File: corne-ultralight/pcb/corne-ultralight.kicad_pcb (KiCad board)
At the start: 2 copper layers, 275.5 x 105.6 mm, 132 parts, among them J2 OLED, J5 Breakaway_Tabs, J7 OLED, SW1 SW_PUSH, SW10 SW_PUSH, SW11 SW_PUSH, SW12 SW_PUSH, SW13 SW_PUSH, SW14 SW_PUSH, SW15 SW_PUSH, SW16 SW_PUSH, SW17 SW_PUSH, SW18 SW_PUSH, SW19 SW_PUSH, SW2 SW_PUSH, SW20 SW_PUSH, SW21 SW_PUSH, SW22 SW_PUSH, SW23 SW_PUSH, SW24 SW_PUSH, SW25 SW_PUSH, SW26 SW_PUSH, SW27 SW_PUSH, SW28 SW_PUSH, SW29 SW_PUSH, SW3 SW_PUSH, SW30 SW_PUSH, SW31 SW_PUSH, SW32 SW_PUSH, SW33 SW_PUSH, SW34 SW_PUSH, SW35 SW_PUSH, SW36 SW_PUSH, SW37 SW_PUSH, SW38 SW_PUSH, SW39 SW_PUSH, SW4 SW_PUSH, SW40 SW_PUSH, SW41 SW_PUSH, SW42 SW_PUSH, SW5 SW_PUSH, SW6 SW_PUSH, SW7 SW_PUSH, SW8 SW_PUSH, SW9 SW_PUSH, U1 ProMicro, U2 ProMicro

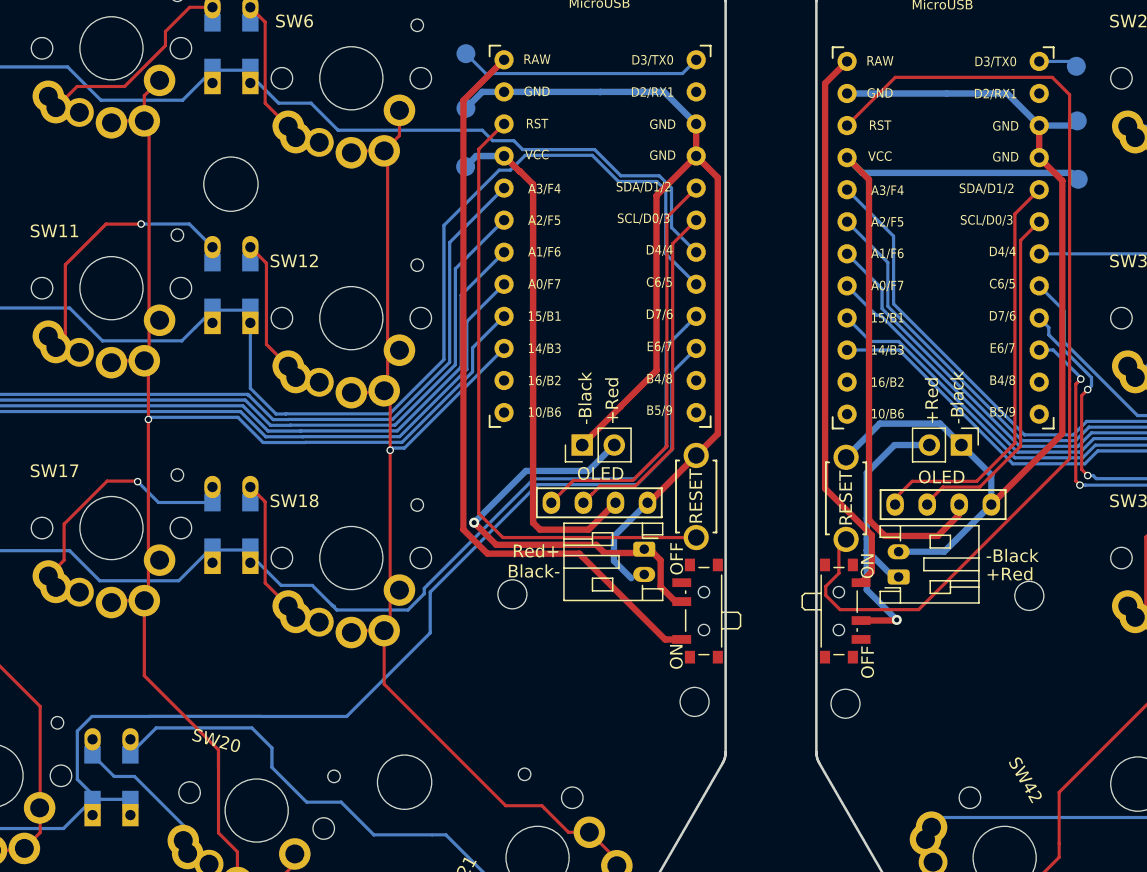
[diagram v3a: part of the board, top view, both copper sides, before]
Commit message: Switch to nice!view display header.
* Route extra pin and move header to be centered for
  nice!view display support.
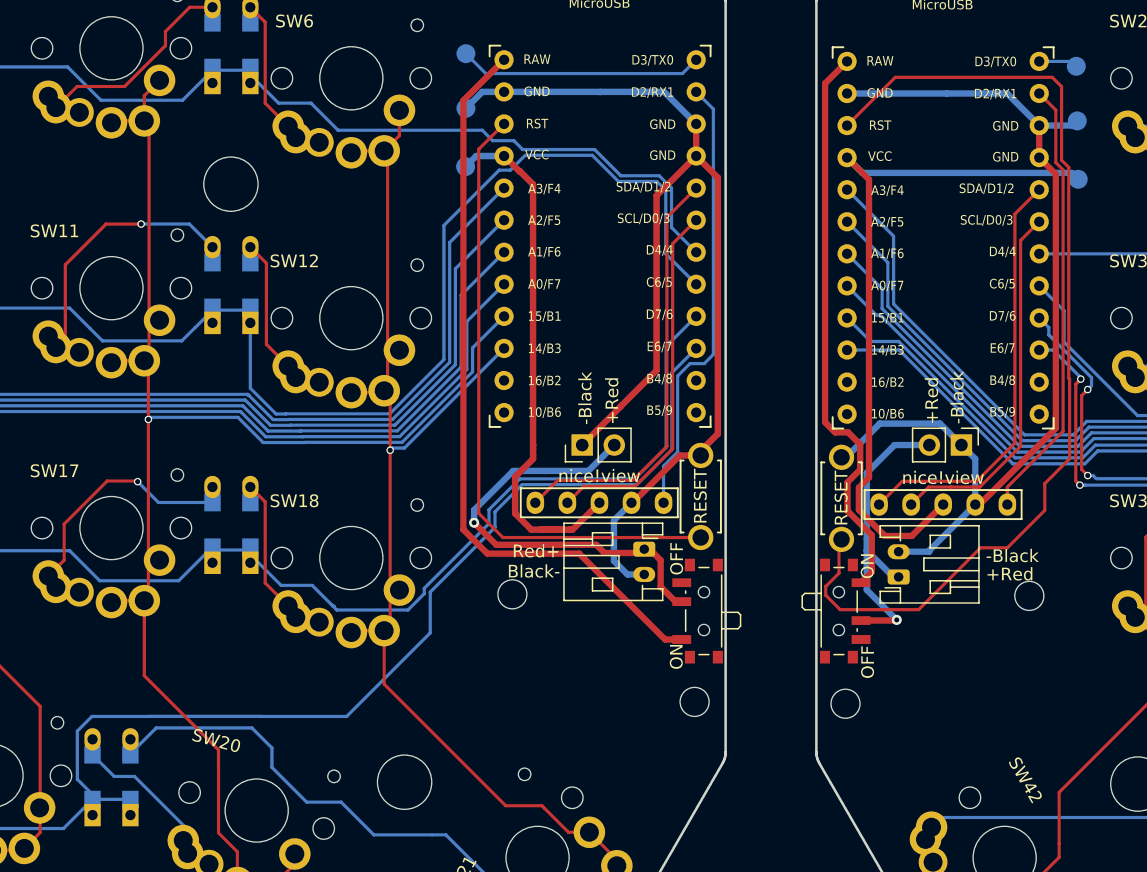
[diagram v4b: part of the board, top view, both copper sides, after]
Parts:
- J2, J7: footprint kbd:OLED_1side -> nice_view:nice_view_1side
- moved J2 1.27 mm to (131.8, 77.2)
- moved J7 1.27 mm to (159.0, 77.3)
- moved RSW2 0.36 mm to (156.0, 76.8)
- moved RSW1 0.36 mm to (144.9, 76.7)
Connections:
- U1 pad 2: unconnected-(U1-Pad2) -> CS
- U2 pad 2: unconnected-(U2-Pad2) -> CS_r
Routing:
- net CS: track 0.00 -> 35.4 mm
- net CS_r: track 0.00 -> 35.2 mm
- net VCC: track 41.1 -> 43.1 mm
- net GND: track 87.2 -> 88.9 mm
- net GNDA: track 78.1 -> 76.6 mm
- net +BATTA: track 43.9 -> 45.3 mm
- net SCL: track 27.7 -> 29.0 mm
- net SDA: track 32.4 -> 33.7 mm
- net reset_r: track 78.4 -> 79.7 mm
- net VDD: track 57.7 -> 56.5 mm
- net SCL_r: track 27.9 -> 29.0 mm
- net SDA_r: track 32.7 -> 33.6 mm
- net row3: track 97.3 -> 98.1 mm
- net row2: track 157.9 -> 158.6 mm
- net Net-(BATJ1-Pad2): track 33.9 -> 34.5 mm

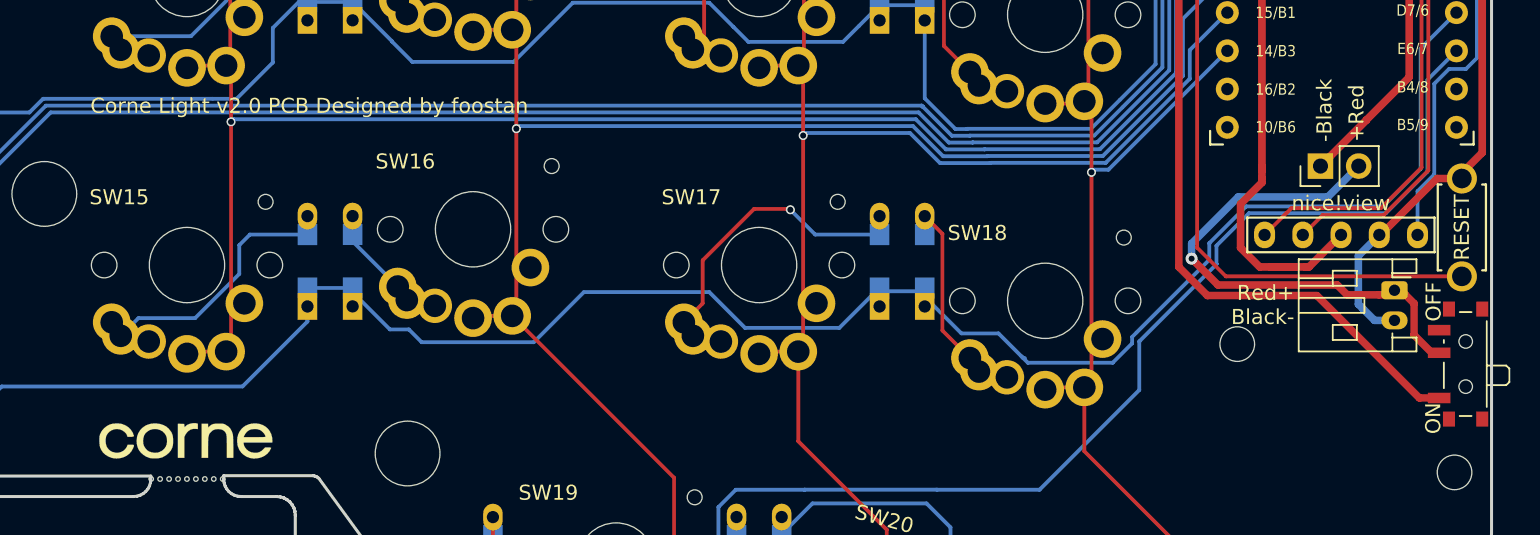
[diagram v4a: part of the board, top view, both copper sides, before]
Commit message: Consistent power switch on/off direction.
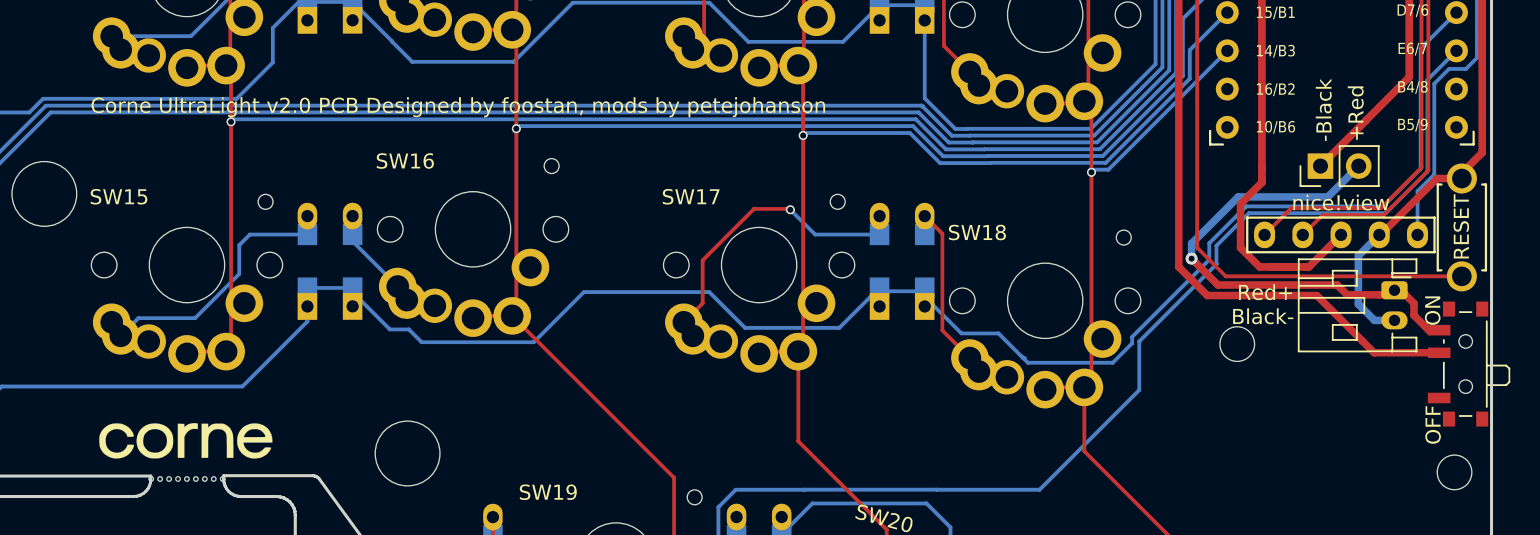
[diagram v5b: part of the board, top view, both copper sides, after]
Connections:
- PSW1 pad 1: +BATT -> unconnected-(PSW1-Pad1)
- PSW1 pad 2: Net-(BATJ1-Pad2) -> +BATT
- PSW1 pad 3: (no net) -> Net-(BATJ1-Pad2)
- PSW2 pad 3: (no net) -> unconnected-(PSW2-Pad3)
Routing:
- net Net-(BATJ1-Pad2): track 34.5 -> 33.1 mm
- net +BATT: track 59.4 -> 58.2 mm
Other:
- board text added: "Corne UltraLight v2.0 PCB Designed by foostan, mods by petejohanson"
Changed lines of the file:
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@@
   (net 87 "+BATTA")
   (net 88 "Net-(BATJ3-Pad2)")
+  (net 89 "unconnected-(PSW1-Pad1)")
+  (net 90 "unconnected-(PSW2-Pad3)")
   (footprint "kbd:ResetSW_1side" (layer "F.Cu")
     (at 156.0125 76.817432 -90)
@@
     (pad "2" smd rect (at 0.75 -1.43 270) (size 0.7 1.5) (layers "F.Cu" "F.Paste" "F.Mask")
       (net 88 "Net-(BATJ3-Pad2)") (pinfunction "B") (pintype "passive"))
-    (pad "3" smd rect (at 2.25 -1.43 270) (size 0.7 1.5) (layers "F.Cu" "F.Paste" "F.Mask"))
+    (pad "3" smd rect (at 2.25 -1.43 270) (size 0.7 1.5) (layers "F.Cu" "F.Paste" "F.Mask")
+      (net 90 "unconnected-(PSW2-Pad3)") (pinfunction "C") (pintype "passive+no_connect"))
     (model "${KICAD6_3DMODEL_DIR}/Button_Switch_SMD.3dshapes/SW_SPDT_PCM12.wrl"
       (offset (xyz 0 0 0))
@@
     (pad "" np_thru_hole circle (at -1.5 0.33 90) (size 0.9 0.9) (drill 0.9) (layers *.Cu *.Mask))
     (pad "1" smd rect (at -2.25 -1.43 90) (size 0.7 1.5) (layers "F.Cu" "F.Paste" "F.Mask")
-      (net 38 "+BATT") (pinfunction "A") (pintype "passive"))
+      (net 89 "unconnected-(PSW1-Pad1)") (pinfunction "A") (pintype "passive+no_connect"))
     (pad "2" smd rect (at 0.75 -1.43 90) (size 0.7 1.5) (layers "F.Cu" "F.Paste" "F.Mask")
-      (net 37 "Net-(BATJ1-Pad2)") (pinfunction "B") (pintype "passive"))
-    (pad "3" smd rect (at 2.25 -1.43 90) (size 0.7 1.5) (layers "F.Cu" "F.Paste" "F.Mask"))
+      (net 38 "+BATT") (pinfunction "B") (pintype "passive"))
+    (pad "3" smd rect (at 2.25 -1.43 90) (size 0.7 1.5) (layers "F.Cu" "F.Paste" "F.Mask")
+      (net 37 "Net-(BATJ1-Pad2)") (pinfunction "C") (pintype "passive"))
     (model "${KICAD6_3DMODEL_DIR}/Button_Switch_SMD.3dshapes/SW_SPDT_PCM12.wrl"
       (offset (xyz 0 0 0))
@@
     (effects (font (size 1 1) (thickness 0.125)) (justify left))
   )
-  (gr_text "Corne Light v2.0 PCB Designed by foostan" (at 53.7675 68.6) (layer "F.SilkS")
+  (gr_text "Corne UltraLight v2.0 PCB Designed by foostan, mods by petejohanson" (at 53.7675 68.6) (layer "F.SilkS")
     (effects (font (size 1 1) (thickness 0.125)) (justify left))
   )
@@
     (effects (font (size 1 1) (thickness 0.15)) (justify left))
   )
-  (gr_text "ON" (at 142.9625 88.295 90) (layer "F.SilkS")
-    (effects (font (size 1 1) (thickness 0.15)) (justify right))
+  (gr_text "ON" (at 142.9625 83.22 90) (layer "F.SilkS")
+    (effects (font (size 1 1) (thickness 0.15)) (justify left))
   )
   (gr_text "Black-" (at 133.7375 82.62) (layer "F.SilkS")
@@
     (effects (font (size 1 1) (thickness 0.15)) (justify left))
   )
-  (gr_text "OFF" (at 142.9875 80.27 90) (layer "F.SilkS")
-    (effects (font (size 1 1) (thickness 0.15)) (justify right))
+  (gr_text "OFF" (at 142.9875 91.12 90) (layer "F.SilkS")
+    (effects (font (size 1 1) (thickness 0.15)) (justify left))
   )
   (segment (start 30.1875 48.916875) (end 30.1875 47.691875) (width 0.25) (layer "B.Cu") (net 1))
@@
   (segment (start 144.5039 52.242) (end 142.1845 54.5614) (width 0.254) (layer "F.Cu") (net 36))
   (segment (start 133.5325 75.394) (end 131.7585 77.168) (width 0.254) (layer "F.Cu") (net 36))
-  (segment (start 141.6875 83.82) (end 142.8625 84.995) (width 0.5) (layer "F.Cu") (net 37))
   (segment (start 136.59002 80.49752) (end 128.66502 80.49752) (width 0.5) (layer "F.Cu") (net 37))
   (segment (start 139.3625 81.145) (end 137.2375 81.145) (width 0.5) (layer "F.Cu") (net 37))
+  (segment (start 142.6625 83.495) (end 141.6875 82.52) (width 0.5) (layer "F.Cu") (net 37))
   (segment (start 139.3625 81.145) (end 141.1125 81.145) (width 0.5) (layer "F.Cu") (net 37))
-  (segment (start 142.8625 84.995) (end 143.3575 84.995) (width 0.5) (layer "F.Cu") (net 37))
-  (segment (start 141.6875 81.72) (end 141.6875 83.82) (width 0.5) (layer "F.Cu") (net 37))
   (segment (start 141.1125 81.145) (end 141.6875 81.72) (width 0.5) (layer "F.Cu") (net 37))
+  (segment (start 141.6875 81.72) (end 141.6875 82.52) (width 0.5) (layer "F.Cu") (net 37))
   (segment (start 137.2375 81.145) (end 136.59002 80.49752) (width 0.5) (layer "F.Cu") (net 37))
+  (segment (start 143.3575 83.495) (end 142.6625 83.495) (width 0.5) (layer "F.Cu") (net 37))
   (segment (start 128.66502 80.49752) (end 126.9125 78.745) (width 0.5) (layer "F.Cu") (net 37))
   (via (at 126.9125 78.745) (size 0.8) (drill 0.4) (layers "F.Cu" "B.Cu") (net 37))
@@
   (segment (start 135.9625 74.645) (end 138.0125 72.595) (width 0.5) (layer "B.Cu") (net 37))
   (segment (start 135.23954 81.19704) (end 127.96246 81.19704) (width 0.5) (layer "F.Cu") (net 38))
+  (segment (start 143.3575 84.995) (end 139.0375 84.995) (width 0.5) (layer "F.Cu") (net 38))
   (segment (start 127.96246 81.19704) (end 126.062989 79.297569) (width 0.5) (layer "F.Cu") (net 38))
-  (segment (start 143.3575 87.995) (end 142.0375 87.995) (width 0.5) (layer "F.Cu") (net 38))
   (segment (start 126.062989 45.302911) (end 129.2839 42.082) (width 0.5) (layer "F.Cu") (net 38))
-  (segment (start 142.0375 87.995) (end 135.23954 81.19704) (width 0.5) (layer "F.Cu") (net 38))
+  (segment (start 139.0375 84.995) (end 138.275 84.2325) (width 0.5) (layer "F.Cu") (net 38))
   (segment (start 126.062989 79.297569) (end 126.062989 45.302911) (width 0.5) (layer "F.Cu") (net 38))
+  (segment (start 138.275 84.2325) (end 135.23954 81.19704) (width 0.5) (layer "F.Cu") (net 38))
   (segment (start 273.684847 49.720432) (end 270.684847 46.720432) (width 0.25) (layer "F.Cu") (net 41))
   (segment (start 270.684847 46.720432) (end 270.684847 42.920432) (width 0.25) (layer "F.Cu") (net 41))

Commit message: Fix hybrid footprint for 5-pin MX switches.
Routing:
- net Net-(D8-Pad2): track 22.1 -> 8.17 mm
- net col0: track 181.9 -> 177.7 mm
- net col1_r: track 165.8 -> 161.7 mm
- net col4: track 116.4 -> 112.2 mm
- net Net-(D29-Pad2): track 27.1 -> 23.0 mm
- net col2_r: track 147.4 -> 143.5 mm
- net col5_r: track 119.5 -> 115.8 mm
- net col4_r: track 133.0 -> 129.4 mm
- net col5: track 94.4 -> 91.2 mm
- net row1_r: track 136.6 -> 139.8 mm
- net col3_r: track 152.8 -> 149.9 mm
- net col1: track 150.3 -> 147.7 mm
- net col3: track 135.1 -> 132.6 mm
- net col0_r: track 188.1 -> 185.7 mm
- net col2: track 126.5 -> 124.1 mm
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
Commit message: feat: switch to hotswap
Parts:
- SW1, SW10, SW11, SW12, SW13, SW14, SW15, SW16, SW17, SW18, SW19, SW2, SW20, SW22, SW23, SW24, SW25, SW26, SW27, SW28, SW29, SW3, SW30, SW31, SW32, SW33, SW34, SW35, SW36, SW37, SW38, SW39, SW4, SW40, SW41, SW5, SW6, SW7, SW8, SW9: footprint gateron-ks27:gateron-ks27-choc-v1-mx -> PCM_Switch_Keyboard_Hotswap_Kailh:SW_Hotswap_Kailh_Choc_V1V2
- SW21, SW42: footprint gateron-ks27:gateron-ks27-choc-v1-mx-1.5u -> PCM_Switch_Keyboard_Hotswap_Kailh:SW_Hotswap_Kailh_Choc_V1V2_1.50u
- moved D16 4.97 mm to (71.2, 73.9)
- moved D10 4.97 mm to (71.2, 54.9)
- moved D4 4.97 mm to (71.2, 35.9)
- moved TP6 3.53 mm to (174.7, 50.4)
- moved D34 2.98 mm to (270.7, 80.9)
- moved D38 2.98 mm to (194.7, 75.9)
- moved D28 2.98 mm to (270.7, 61.9)
- moved D22 2.98 mm to (270.7, 42.9)
- moved D2 2.98 mm to (33.2, 42.9)
- moved D19 2.97 mm to (80.7, 95.9)
- moved D41 2.97 mm to (204.2, 95.9)
- moved D8 2.75 mm to (33.2, 62.2)
- moved D30 2.70 mm to (232.7, 57.2)
- moved D14 2.70 mm to (33.2, 81.2)
- moved D36 2.48 mm to (232.7, 76.4)
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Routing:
- net row1: track 168.5 -> 147.9 mm
- net col0: track 177.7 -> 163.3 mm, vias 1 -> 4
- net Net-(D37-Pad2): track 14.2 -> 24.3 mm
- net row3: track 97.9 -> 88.4 mm
- net Net-(D23-Pad2): track 18.0 -> 27.3 mm, vias 0 -> 1
- net Net-(D5-Pad2): track 17.6 -> 26.3 mm, vias 0 -> 2
- net row2: track 157.3 -> 148.9 mm
- net col3_r: track 149.9 -> 158.1 mm, vias 1 -> 5
- net col4_r: track 129.4 -> 137.4 mm, vias 1 -> 5
- net Net-(D25-Pad2): track 17.3 -> 24.3 mm
- net Net-(D31-Pad2): track 17.4 -> 24.3 mm
- net col1: track 147.7 -> 140.9 mm, vias 1 -> 4
- net col0_r: track 185.7 -> 192.5 mm, vias 1 -> 4
- net Net-(D17-Pad2): track 19.7 -> 26.0 mm, vias 1 -> 2
- net col5: track 91.2 -> 85.4 mm, vias 1 -> 5
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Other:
- outline, holes or cut-outs redrawn

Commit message: fix: correct the routing problem
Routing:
- net col4_r: track 137.4 -> 127.7 mm, vias 5 -> 7
- net col5_r: track 120.2 -> 111.2 mm, vias 5 -> 7
- net col0_r: track 192.5 -> 183.7 mm, vias 4 -> 5
- net col3_r: track 158.1 -> 150.0 mm, vias 5 -> 7
- net col1_r: track 165.1 -> 157.7 mm, vias 4 -> 5
- net col3: track 129.8 -> 122.5 mm, vias 5 -> 7
- net col2: track 123.0 -> 116.3 mm, vias 4 -> 5
- net col0: track 163.3 -> 168.4 mm
- net col4: track 108.9 -> 105.0 mm, vias 5 -> 7
- net col2_r: track 140.2 -> 137.8 mm, vias 4 -> 5
- net col1: track 140.9 -> 138.8 mm
- net col5: track 85.4 -> 86.4 mm, vias 5 -> 7
